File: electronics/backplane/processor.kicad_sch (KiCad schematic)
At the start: 23 parts, among them P6 PAD_SOLDER_2mm, P7 PAD_SOLDER_2mm, P8 PAD_SOLDER_2mm, P9 PAD_SOLDER_2mm, SW1 B3U-1000P_SPST-NO_SMD, SW2 B3U-1000P_SPST-NO_SMD, X1 MICROMOD_PROCESSOR_SOCKET, X2 SWD_SMT_SOCKET

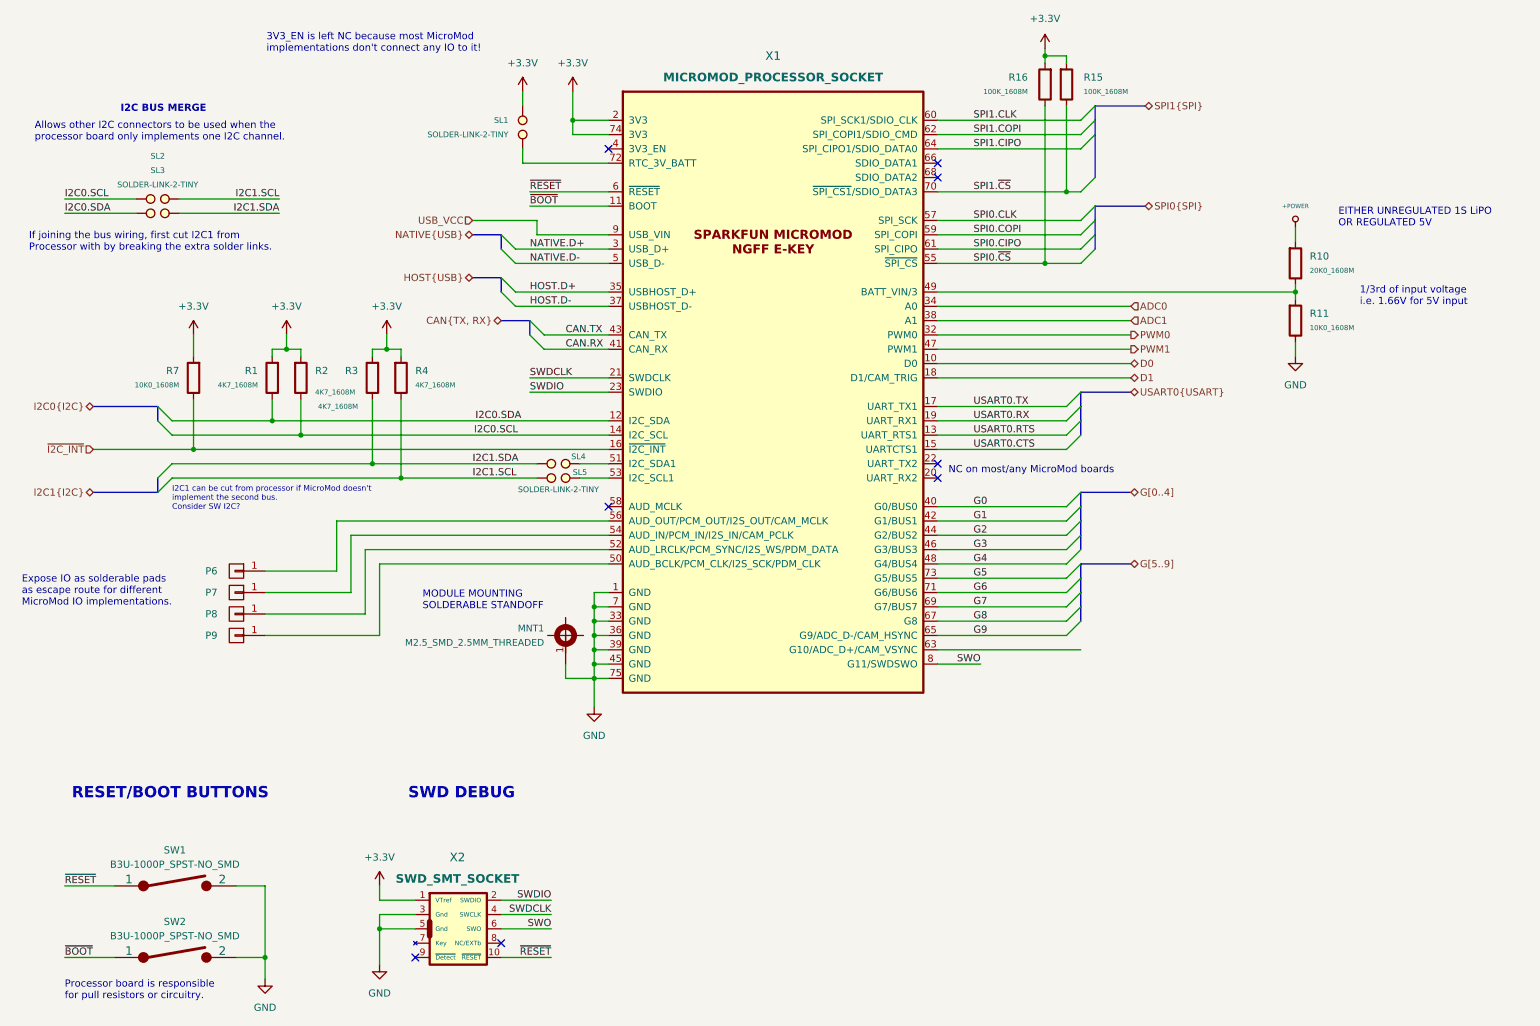
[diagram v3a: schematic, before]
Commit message: Backplane routing complete General schematic cleanup, board cosmetics etc
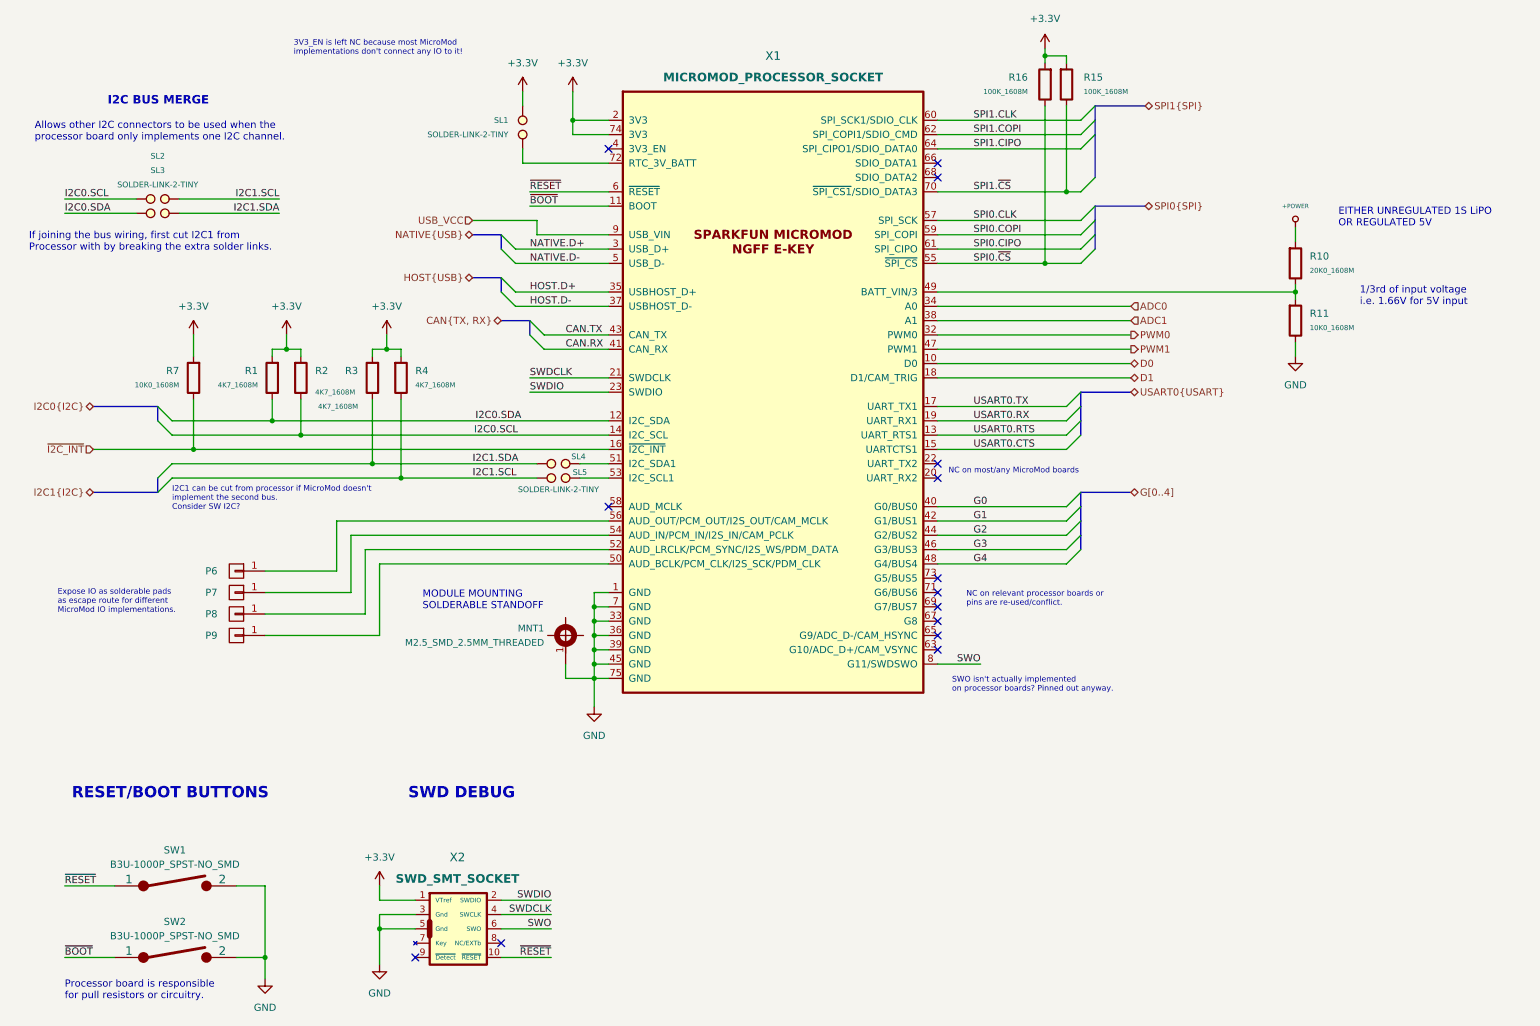
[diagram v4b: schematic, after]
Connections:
- net G5: no longer names the net of X1.73 (G5/BUS5)
- net G6: no longer names the net of X1.71 (G6/BUS6)
- net G7: no longer names the net of X1.69 (G7/BUS7)
- net G8: no longer names the net of X1.67 (G8)
- net G9: no longer names the net of X1.65 (G9/ADC_D-/CAM_HSYNC)
- no-connect marks 8 -> 14
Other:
- note added: "NC on relevant processor boards or pins are re-used/conflict."
- note added: "SWO isn't actually implemented on processor boards? Pinned out anyway."
- title: (none) -> MicroMod Processor
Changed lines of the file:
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@@
 (kicad_sch (version 20230121) (generator eeschema)
   (paper "A4")
+  (title_block
+    (title "MicroMod Processor")
+    (date "2023-08-09")
+    (rev "V1.0")
+    (comment 1 "Check processor and function board compatibility before use!")
+    (comment 3 "Designed with ESP32, STM32, RP2040 as targets")
+    (comment 4 "Supports Sparkfun MicroMod hardware")
+  )
   (junction (at 62.23 85.09) (diameter 0) (color 0 0 0 0)
   )
@@
   (no_connect (at 180.34 41.91))
   (no_connect (at 121.92 36.83))
+  (no_connect (at 180.34 115.57))
   (no_connect (at 180.34 95.25))
+  (no_connect (at 180.34 118.11))
   (no_connect (at 180.34 92.71))
+  (no_connect (at 180.34 113.03))
+  (no_connect (at 180.34 123.19))
   (no_connect (at 180.34 39.37))
+  (no_connect (at 180.34 125.73))
   (no_connect (at 121.92 100.33))
   (no_connect (at 102.87 177.8))
+  (no_connect (at 180.34 120.65))
   (bus_entry (at 44.45 87.63) (size -2.54 -2.54)
     (stroke (width 0) (type default))
@@
     (stroke (width 0) (type default))
   )
-  (bus_entry (at 203.2 113.03) (size 2.54 -2.54)
-    (stroke (width 0) (type default))
-  )
   (bus_entry (at 205.74 44.45) (size 2.54 -2.54)
     (stroke (width 0) (type default))
   )
-  (bus_entry (at 203.2 120.65) (size 2.54 -2.54)
-    (stroke (width 0) (type default))
-  )
   (bus_entry (at 110.49 69.85) (size -2.54 -2.54)
     (stroke (width 0) (type default))
@@
     (stroke (width 0) (type default))
   )
-  (bus_entry (at 203.2 115.57) (size 2.54 -2.54)
-    (stroke (width 0) (type default))
-  )
   (bus_entry (at 110.49 72.39) (size -2.54 -2.54)
     (stroke (width 0) (type default))
@@
     (stroke (width 0) (type default))
   )
-  (bus_entry (at 203.2 123.19) (size 2.54 -2.54)
-    (stroke (width 0) (type default))
-  )
   (bus_entry (at 203.2 107.95) (size 2.54 -2.54)
     (stroke (width 0) (type default))
@@
     (stroke (width 0) (type default))
   )
-  (bus_entry (at 203.2 118.11) (size 2.54 -2.54)
-    (stroke (width 0) (type default))
-  )
   (bus_entry (at 44.45 92.71) (size -2.54 2.54)
     (stroke (width 0) (type default))
@@
     (stroke (width 0) (type default))
   )
-  (bus (pts (xy 205.74 113.03) (xy 205.74 115.57))
-    (stroke (width 0) (type default))
-  )
   (bus (pts (xy 205.74 105.41) (xy 205.74 107.95))
     (stroke (width 0) (type default))
@@
     (stroke (width 0) (type default))
   )
-  (bus (pts (xy 205.74 115.57) (xy 205.74 118.11))
-    (stroke (width 0) (type default))
-  )
   (wire (pts (xy 109.22 49.53) (xy 109.22 52.07))
     (stroke (width 0) (type default))
@@
     (stroke (width 0) (type default))
   )
-  (bus (pts (xy 205.74 110.49) (xy 214.63 110.49))
-    (stroke (width 0) (type default))
-  )
   (bus (pts (xy 102.87 67.31) (xy 107.95 67.31))
     (stroke (width 0) (type default))
@@
     (stroke (width 0) (type default))
   )
-  (bus (pts (xy 205.74 118.11) (xy 205.74 120.65))
-    (stroke (width 0) (type default))
-  )
   (wire (pts (xy 180.34 107.95) (xy 203.2 107.95))
     (stroke (width 0) (type default))
@@
     (stroke (width 0) (type default))
   )
-  (wire (pts (xy 180.34 120.65) (xy 203.2 120.65))
-    (stroke (width 0) (type default))
-  )
   (wire (pts (xy 67.31 81.28) (xy 67.31 87.63))
     (stroke (width 0) (type default))
@@
     (stroke (width 0) (type default))
   )
-  (bus (pts (xy 205.74 110.49) (xy 205.74 113.03))
-    (stroke (width 0) (type default))
-  )
   (wire (pts (xy 105.41 62.23) (xy 121.92 62.23))
     (stroke (width 0) (type default))
@@
     (stroke (width 0) (type default))
   )
-  (wire (pts (xy 180.34 118.11) (xy 203.2 118.11))
-    (stroke (width 0) (type default))
-  )
   (wire (pts (xy 180.34 128.27) (xy 187.96 128.27))
     (stroke (width 0) (type default))
   )
-  (wire (pts (xy 180.34 123.19) (xy 203.2 123.19))
-    (stroke (width 0) (type default))
-  )
   (wire (pts (xy 62.23 81.28) (xy 62.23 85.09))
     (stroke (width 0) (type default))
@@
     (stroke (width 0) (type default))
   )
-  (wire (pts (xy 180.34 115.57) (xy 203.2 115.57))
-    (stroke (width 0) (type default))
-  )
   (wire (pts (xy 121.92 130.81) (xy 119.38 130.81))
     (stroke (width 0) (type default))
@@
     (stroke (width 0) (type default))
   )
-  (wire (pts (xy 180.34 125.73) (xy 205.74 125.73))
-    (stroke (width 0) (type default))
-  )
   (bus (pts (xy 205.74 82.55) (xy 205.74 80.01))
     (stroke (width 0) (type default))
@@
     (stroke (width 0) (type default))
   )
-  (wire (pts (xy 180.34 113.03) (xy 203.2 113.03))
-    (stroke (width 0) (type default))
-  )
   (wire (pts (xy 64.77 72.39) (xy 67.31 72.39))
     (stroke (width 0) (type default))
@@
   )
   (text "Expose IO as solderable pads\nas escape route for different\nMicroMod IO implementations.\n"
-    (at 17.78 118.11 0)
-    (effects (font (size 1.27 1.27)) (justify left bottom))
+    (at 24.13 119.38 0)
+    (effects (font (size 1 1)) (justify left bottom))
   )
   (text "If joining the bus wiring, first cut I2C1 from \nProcessor with by breaking the extra solder links."
@@
   )
   (text "NC on most/any MicroMod boards" (at 182.245 94.615 0)
-    (effects (font (size 1.27 1.27)) (justify left bottom))
+    (effects (font (size 1 1)) (justify left bottom))
   )
   (text "Processor board is responsible \nfor pull resistors or circuitry."
@@
     (effects (font (size 1 1)) (justify left bottom))
   )
-  (text "I2C BUS MERGE" (at 35.306 30.48 0)
-    (effects (font (size 1.27 1.27) (thickness 0.254) bold) (justify left bottom))
+  (text "I2C BUS MERGE" (at 33.02 29.21 0)
+    (effects (font (size 1.5 1.5) (thickness 0.254) bold) (justify left bottom))
   )
   (text "EITHER UNREGULATED 1S LiPO\nOR REGULATED 5V" (at 251.46 50.8 0)
     (effects (font (size 1.27 1.27)) (justify left bottom))
+  )
+  (text "SWO isn't actually implemented \non processor boards? Pinned out anyway."
+    (at 182.88 133.35 0)
+    (effects (font (size 1 1)) (justify left bottom))
   )
   (text "1/3rd of input voltage\ni.e. 1.66V for 5V input" (at 255.27 64.77 0)
@@
   )
   (text "3V3_EN is left NC because most MicroMod\nimplementations don't connect any IO to it!"
-    (at 61.214 19.812 0)
-    (effects (font (size 1.27 1.27)) (justify left bottom))
+    (at 66.04 20.32 0)
+    (effects (font (size 1 1)) (justify left bottom))
+  )
+  (text "NC on relevant processor boards or\npins are re-used/conflict."
+    (at 185.42 118.11 0)
+    (effects (font (size 1 1)) (justify left bottom))
   )
   (text "Allows other I2C connectors to be used when the \nprocessor board only implements one I2C channel."
@@
     (effects (font (size 1.27 1.27)) (justify left bottom))
   )
-  (label "G5" (at 186.69 113.03 0) (fields_autoplaced)
-    (effects (font (size 1.27 1.27)) (justify left bottom))
-  )
   (label "HOST.D-" (at 107.95 64.77 0) (fields_autoplaced)
     (effects (font (size 1.27 1.27)) (justify left bottom))
@@
     (effects (font (size 1.27 1.27)) (justify left bottom))
   )
-  (label "G9" (at 186.69 123.19 0) (fields_autoplaced)
-    (effects (font (size 1.27 1.27)) (justify left bottom))
-  )
   (label "SPI0.CLK" (at 186.69 49.53 0) (fields_autoplaced)
     (effects (font (size 1.27 1.27)) (justify left bottom))
   )
   (label "G4" (at 186.69 110.49 0) (fields_autoplaced)
-    (effects (font (size 1.27 1.27)) (justify left bottom))
-  )
-  (label "G7" (at 186.69 118.11 0) (fields_autoplaced)
     (effects (font (size 1.27 1.27)) (justify left bottom))
   )
@@
     (effects (font (size 1.27 1.27)) (justify left bottom))
   )
-  (label "G6" (at 186.69 115.57 0) (fields_autoplaced)
-    (effects (font (size 1.27 1.27)) (justify left bottom))
-  )
   (label "SPI1.CLK" (at 186.69 31.75 0) (fields_autoplaced)
     (effects (font (size 1.27 1.27)) (justify left bottom))
@@
     (effects (font (size 1.27 1.27)) (justify left bottom))
   )
-  (label "G8" (at 186.69 120.65 0) (fields_autoplaced)
-    (effects (font (size 1.27 1.27)) (justify left bottom))
-  )
   (label "NATIVE.D+" (at 107.95 54.61 0) (fields_autoplaced)
     (effects (font (size 1.27 1.27)) (justify left bottom))
@@
     (effects (font (size 1.27 1.27)) (justify left))
   )
-  (hierarchical_label "G[5..9]" (shape bidirectional) (at 214.63 110.49 0) (fields_autoplaced)
-    (effects (font (size 1.27 1.27)) (justify left))
-  )
